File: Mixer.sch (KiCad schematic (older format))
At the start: 31 parts, among them J101 AudioJack2, J102 AudioJack2, J103 AudioJack2, J104 AudioJack2, J105 Conn_02x05_Counter_Clockwise, U101 TL074, U102 TL072

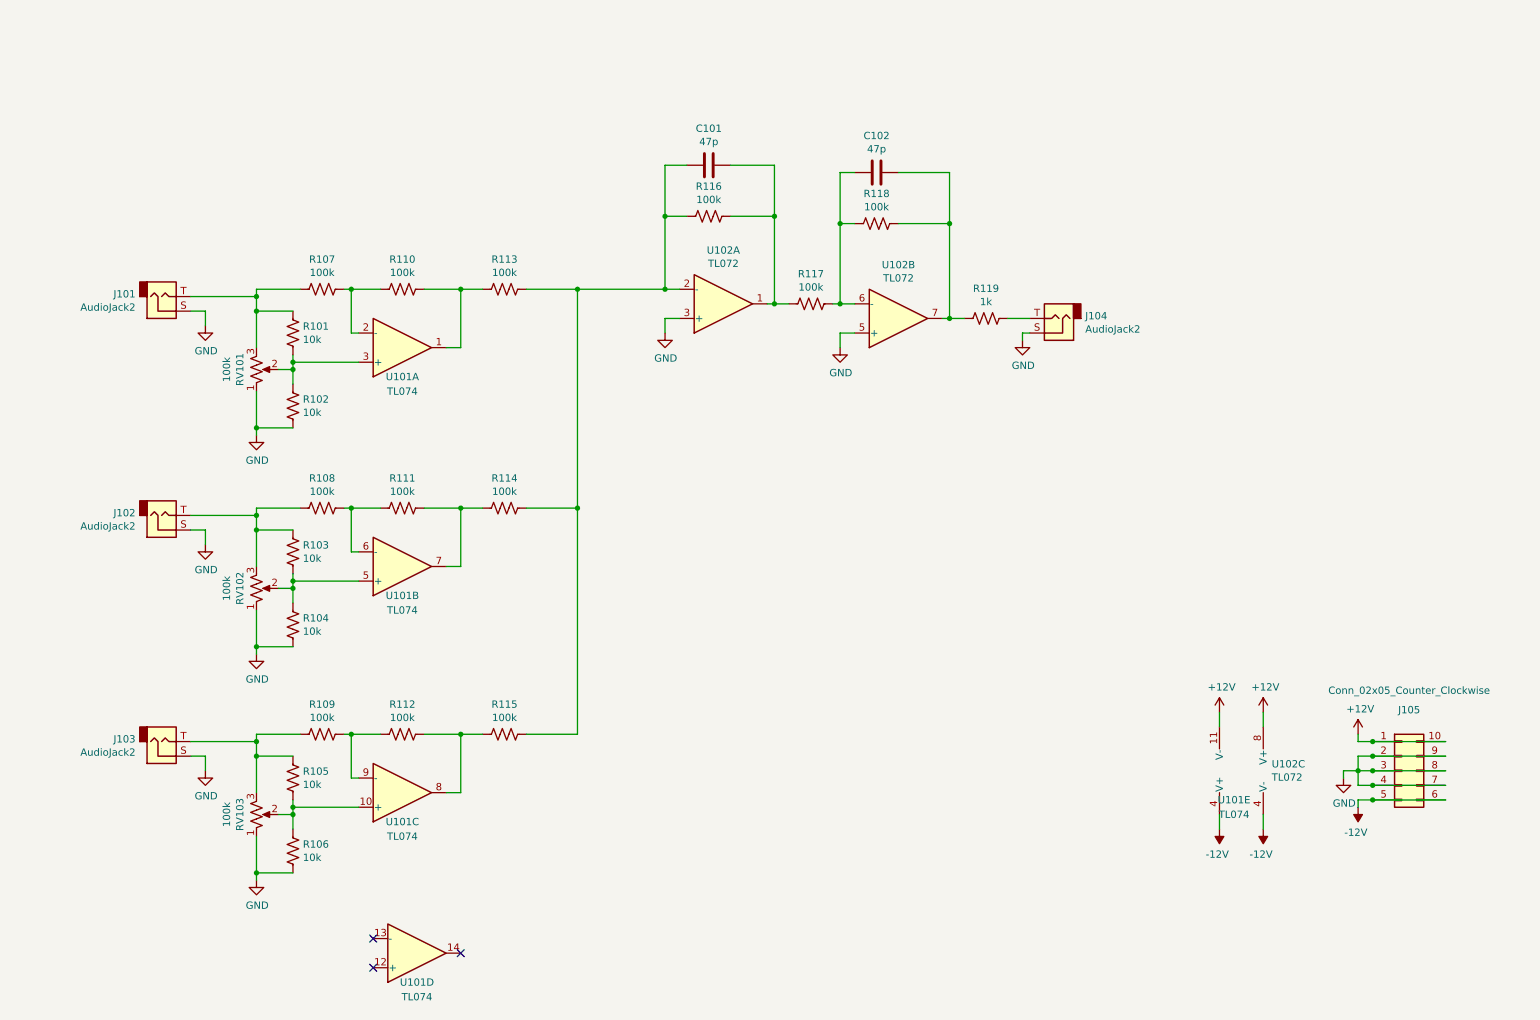
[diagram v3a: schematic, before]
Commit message: fixed op amp issue
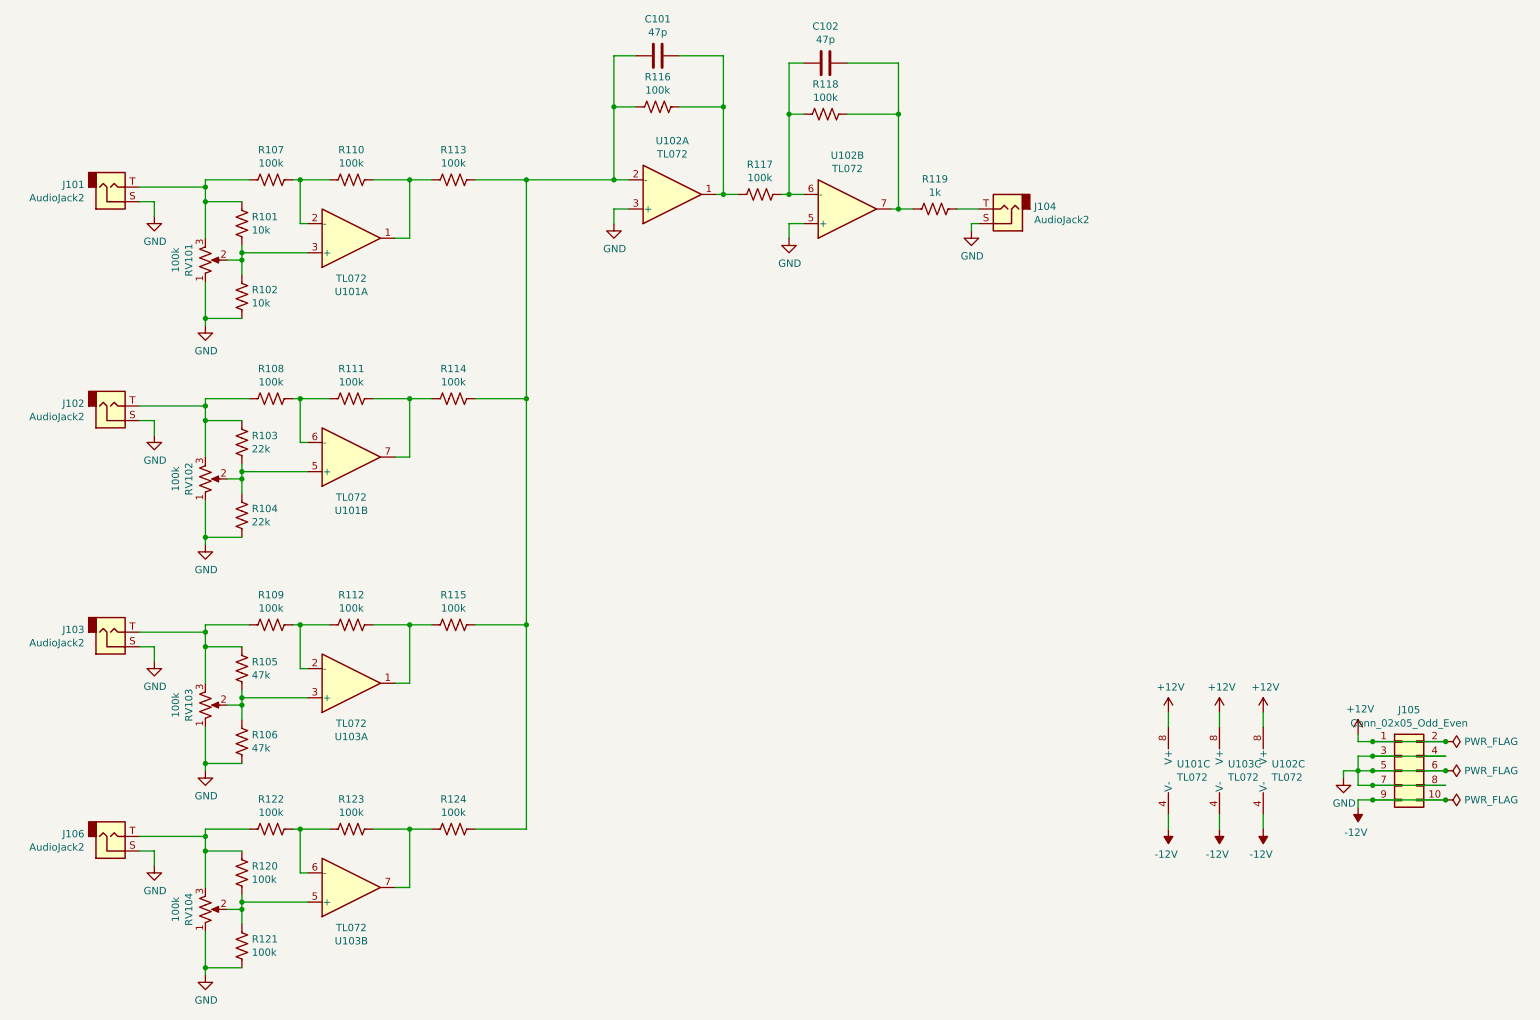
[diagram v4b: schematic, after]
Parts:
- removed J105: Conn_02x05_Counter_Clockwise, Connector_PinHeader_2.54mm:PinHeader_2x05_P2.54mm_Vertical, symbol Connector_Generic:Conn_02x05_Counter_Clockwise
- removed U101: TL074, Package_DIP:DIP-14_W7.62mm, symbol Amplifier_Operational:TL074
- added J105: Conn_02x05_Odd_Even, Connector_PinHeader_2.54mm:PinHeader_2x05_P2.54mm_Vertical, symbol Connector_Generic:Conn_02x05_Odd_Even
- added J106: AudioJack2, A-2563:A-2563, symbol Connector:AudioJack2
- added R120, R121, R122, R123, R124: 100k, Resistor_SMD:R_0805_2012Metric, symbol Device:R_US
- added RV104: 100k, A-5513:A-5513, symbol Device:R_POT_US
- added U101, U103: TL072, Package_SO:SOIC-8_3.9x4.9mm_P1.27mm, symbol Amplifier_Operational:TL072
- R101, R102: footprint Resistor_THT:R_Axial_DIN0207_L6.3mm_D2.5mm_P7.62mm_Horizontal -> Resistor_SMD:R_0805_2012Metric; LCSC (none) -> C17414
- R103, R104: value 10k -> 22k; footprint Resistor_THT:R_Axial_DIN0207_L6.3mm_D2.5mm_P7.62mm_Horizontal -> Resistor_SMD:R_0805_2012Metric; LCSC (none) -> C17560
- R105, R106: value 10k -> 47k; footprint Resistor_THT:R_Axial_DIN0207_L6.3mm_D2.5mm_P7.62mm_Horizontal -> Resistor_SMD:R_0805_2012Metric; LCSC (none) -> C17713
- R119: footprint Resistor_THT:R_Axial_DIN0207_L6.3mm_D2.5mm_P7.62mm_Horizontal -> Resistor_SMD:R_0805_2012Metric; LCSC (none) -> C17513
- U102: footprint Package_DIP:DIP-8_W7.62mm -> Package_SO:SOIC-8_3.9x4.9mm_P1.27mm; LCSC (none) -> C6961
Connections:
- net +12V: now also J105.1 (Pin_1), J105.2 (Pin_2), U101.8 (V+), U103.8 (V+)
- net -12V: now also J105.10 (Pin_10), J105.9 (Pin_9), U101.4 (V-), U103.4 (V-)
- net GND: now also J105.3 (Pin_3), J105.4 (Pin_4), J105.5 (Pin_5), J105.6 (Pin_6), J105.7 (Pin_7), J105.8 (Pin_8), J106.S, R121.2, RV104.1
- net at R101.2, R102.1, RV101.2: now also U101.3 (+)
- net at R107.1, R110.2: now also U101.2 (-)
- net at C101.2, R113.1, R114.1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: now also R124.1
- net at R110.1, R113.2: now also U101.1
- net at R103.2, R104.1, RV102.2: now also U101.5 (+)
- net at R108.1, R111.2: now also U101.6 (-)
- net at R111.1, R114.2: now also U101.7
- net at R105.2, R106.1, RV103.2: now also U103.3 (+)
- net at R109.1, R112.2: now also U103.2 (-)
- net at R112.1, R115.2: now also U103.1
- new net: J106.T, R120.1, R122.2, RV104.3
- new net: R120.2, R121.1, RV104.2, U103.5 (+)
- new net: R122.1, R123.2, U103.6 (-)
- new net: R123.1, R124.2, U103.7
- no-connect marks 3 -> 0
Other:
- moved on the sheet: C101, C102, J101, J102, J103, J104, R101, R102, R103, R104, R105, R106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
